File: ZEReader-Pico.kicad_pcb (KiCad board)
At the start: 2 copper layers, 100 x 110 mm, 75 parts, among them J1 Micro_SD_Card_Det2, J2 UART, J3 SWD, J4 Conn_01x24_MountingPin, J5 UJ20-C-H-G-SMT-TR, J6 Conn_01x02_Socket, Q1 Si1308EDL, Q2 DMG2305UX-7, SW1 SW_Push, SW2 SW_Push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

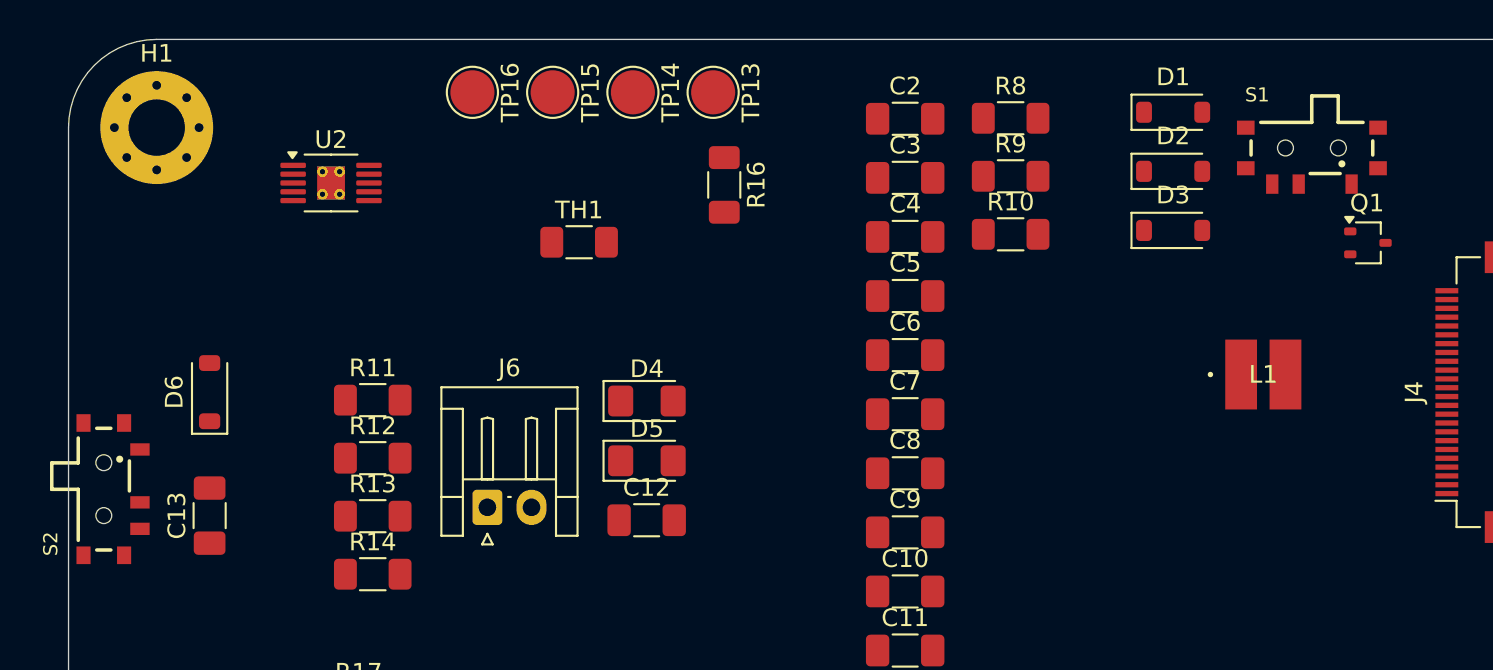
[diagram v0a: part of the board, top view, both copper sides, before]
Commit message: selfcontainment, smaller fixes
Signed-off-by: Anna-Lena Marx <anna-lena.marx@web.de>
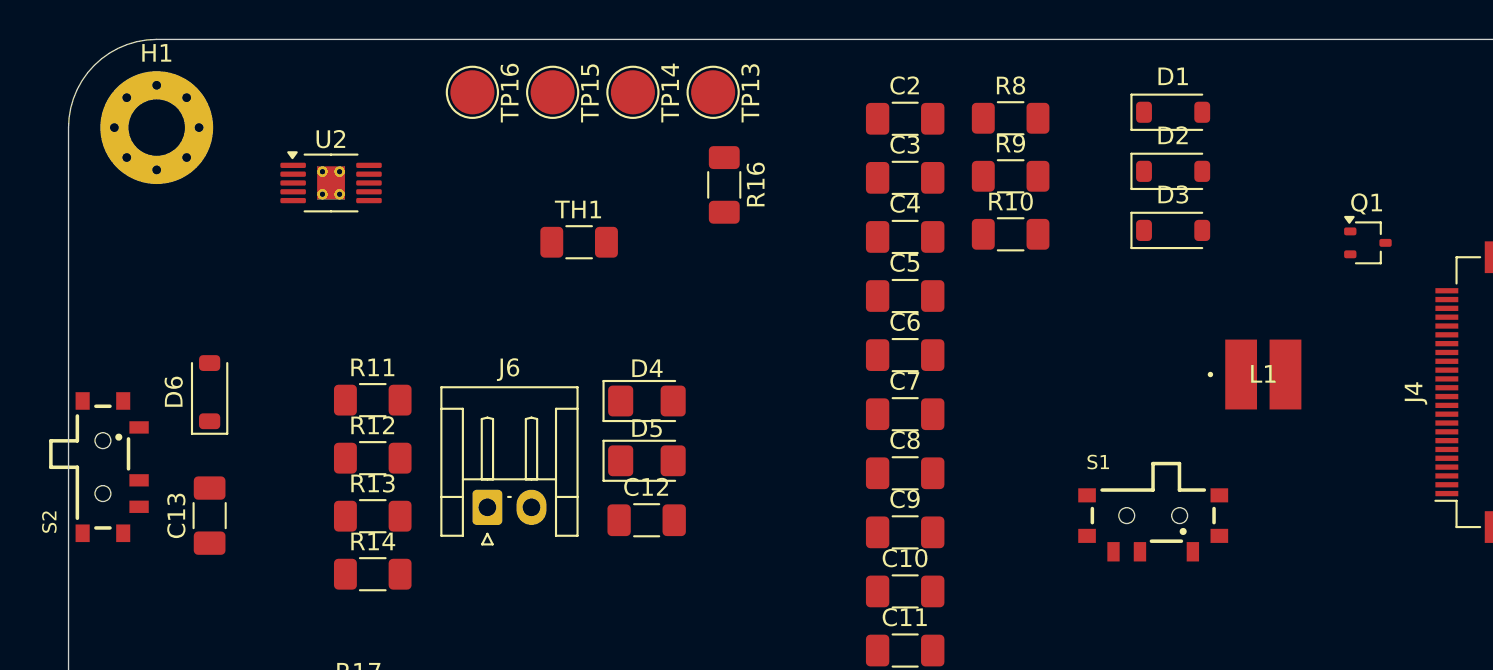
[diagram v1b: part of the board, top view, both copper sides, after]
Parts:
- moved S1 22.7 mm to (111.5, 52.0)
- moved S2 1.25 mm to (52.0, 49.2)

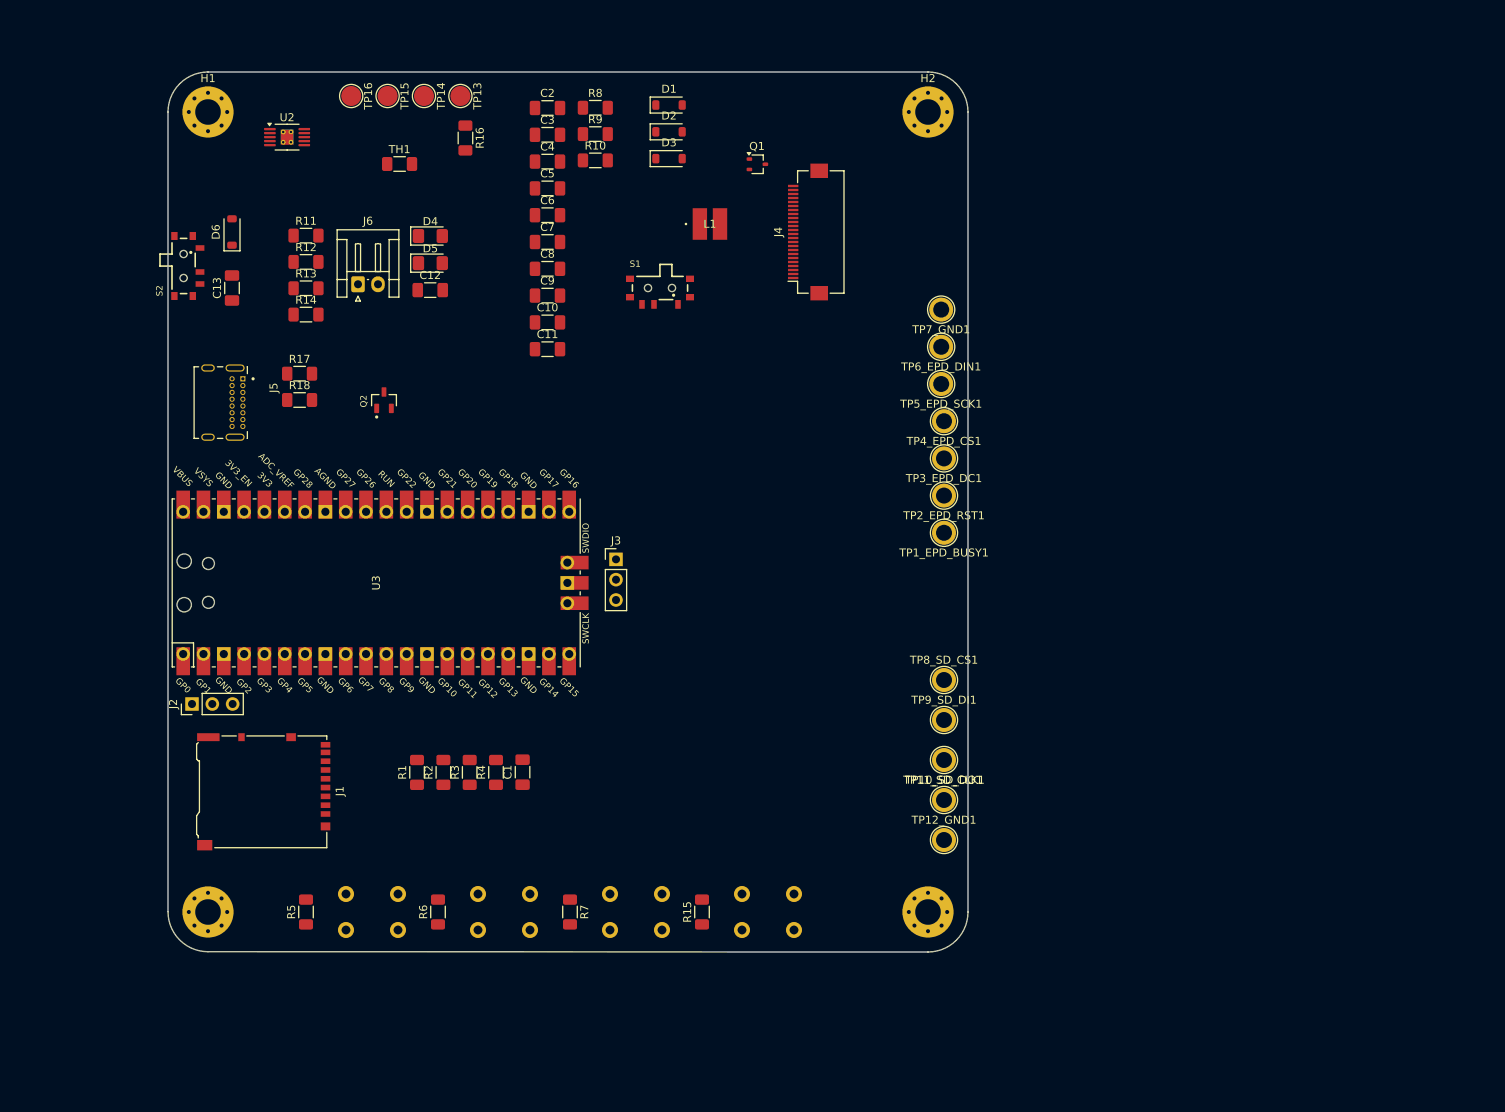
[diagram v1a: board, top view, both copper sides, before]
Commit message: Imported Aisler design rules, routed power and display booster
Signed-off-by: Anna-Lena Marx <anna-lena.marx@web.de>
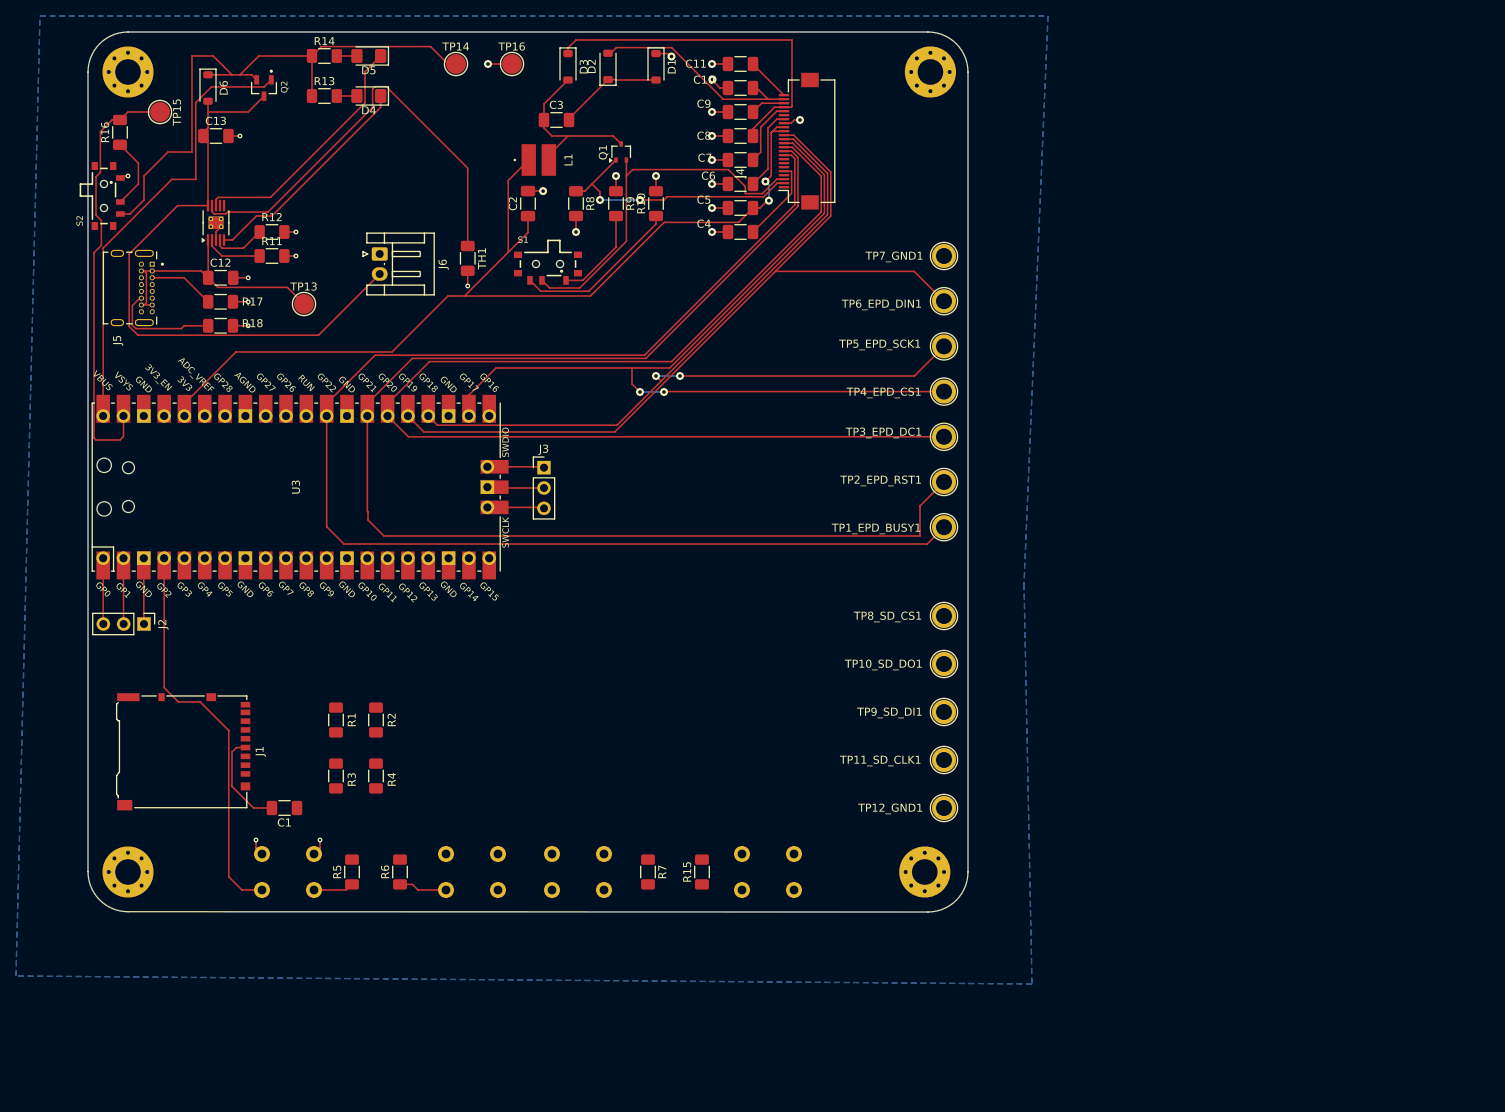
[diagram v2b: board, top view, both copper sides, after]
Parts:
- moved R16 43.2 mm to (44.0, 32.5), turned to 90 degrees
- moved C11 43.0 mm to (121.6, 24.0)
- moved Q2 41.8 mm to (62.0, 27.0), turned to -90 degrees
- moved C10 38.0 mm to (121.6, 27.0)
- moved C9 33.3 mm to (121.6, 30.0)
- moved TP13 32.5 mm to (67.0, 54.0), turned to 0 degrees
- moved R14 32.4 mm to (69.5, 23.0)
- moved C1 30.1 mm to (64.6, 117.0), turned to 180 degrees
- moved C8 29.3 mm to (121.6, 33.0)
- moved TP15 28.5 mm to (49.0, 30.0)
- moved D5 27.0 mm to (75.1, 23.0), turned to 180 degrees
- moved C12 26.2 mm to (56.6, 50.7)
- moved C7 26.2 mm to (121.6, 36.0)
- moved C4 25.7 mm to (121.6, 45.0)
- moved C6 24.4 mm to (121.6, 39.0)
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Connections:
- J2 pad 1: Net-(J2-Pin_1) -> GND
- J2 pad 3: GND -> Net-(J2-Pin_3)
- J6 pad 1: /02_Power/V_USB_LIPO -> GND
- J6 pad 2: GND -> /02_Power/V_USB_LIPO
- U3 pad 1: Net-(J2-Pin_1) -> Net-(J2-Pin_3)
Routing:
- net EPD_BUSY: track 0.00 -> 170.4 mm
- net EPD_RST: track 0.00 -> 164.6 mm
- net /02_Power/V_USB_LIPO: track 0.00 -> 150.3 mm
- net EPD_DC: track 0.00 -> 146.9 mm
- net +3.3V: track 0.00 -> 123.6 mm, vias 0 -> 2
- net EPD_SCK: track 0.00 -> 112.1 mm, vias 0 -> 2
- net EPD_CS: track 0.00 -> 109.4 mm, vias 0 -> 2
- net EPD_DIN: track 0.00 -> 100.7 mm
- net GND: track 0.00 -> 67.5 mm, vias 0 -> 25
- net VBUS: track 0.00 -> 56.3 mm
- net Net-(U2-TS): track 0.00 -> 54.7 mm
- net BTN_1: track 0.00 -> 54.6 mm
- net VSYS: track 0.00 -> 54.2 mm
- net /03_ePaper-Driver/RESE: track 0.00 -> 46.1 mm
- net /03_ePaper-Driver/VGH: track 0.00 -> 44.3 mm
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- added copper zone on B.Cu, net GND
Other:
- board size 100 x 110 mm -> 110 x 110 mm

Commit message: Initial routing finished
Signed-off-by: Anna-Lena Marx <anna-lena.marx@web.de>
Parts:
- moved C1 23.0 mm to (63.4, 94.0), turned to 0 degrees
- moved R5 15.0 mm to (58.0, 125.5)
- moved R3 12.5 mm to (72.0, 100.5), turned to -90 degrees
- moved R4 12.5 mm to (75.5, 100.5), turned to -90 degrees
- moved R2 9.28 mm to (68.5, 100.5), turned to -90 degrees
- moved R1 8.11 mm to (65.0, 100.5), turned to -90 degrees
- moved R15 0.60 mm to (117.0, 125.5), turned to -90 degrees
- moved R6 0.55 mm to (79.0, 125.5)
- moved R7 0.55 mm to (110.0, 125.5)
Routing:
- net +3.3V: track 123.6 -> 314.2 mm
- net SD_DAT3-CD-CS: track 0.00 -> 140.4 mm
- net SD_CLK-SCLK: track 0.00 -> 134.6 mm
- net BTN_4: track 0.00 -> 129.2 mm
- net SD_CMD-DI: track 0.00 -> 125.7 mm
- net BTN_3: track 0.00 -> 124.0 mm
- net SD_DAT0-DO: track 0.00 -> 115.4 mm, vias 0 -> 2
- net BTN_2: track 6.04 -> 95.2 mm
- net Net-(J1-VDD): track 12.3 -> 54.1 mm
- net GND: track 67.5 -> 85.6 mm, vias 25 -> 33
- net BTN_1: track 54.6 -> 64.3 mm
- net EPD_RST: track 164.6 -> 163.5 mm
- net Net-(D5-K): track 31.1 -> 31.6 mm
- net EPD_BUSY: track 170.4 -> 171.0 mm
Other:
- board text added: "ZEReader Pico v1 Git Rev: ${kibot_git-hash} Anna-Lena Marx"
- board text removed: "v1 Git Rev: ${kibot_git-hash}"

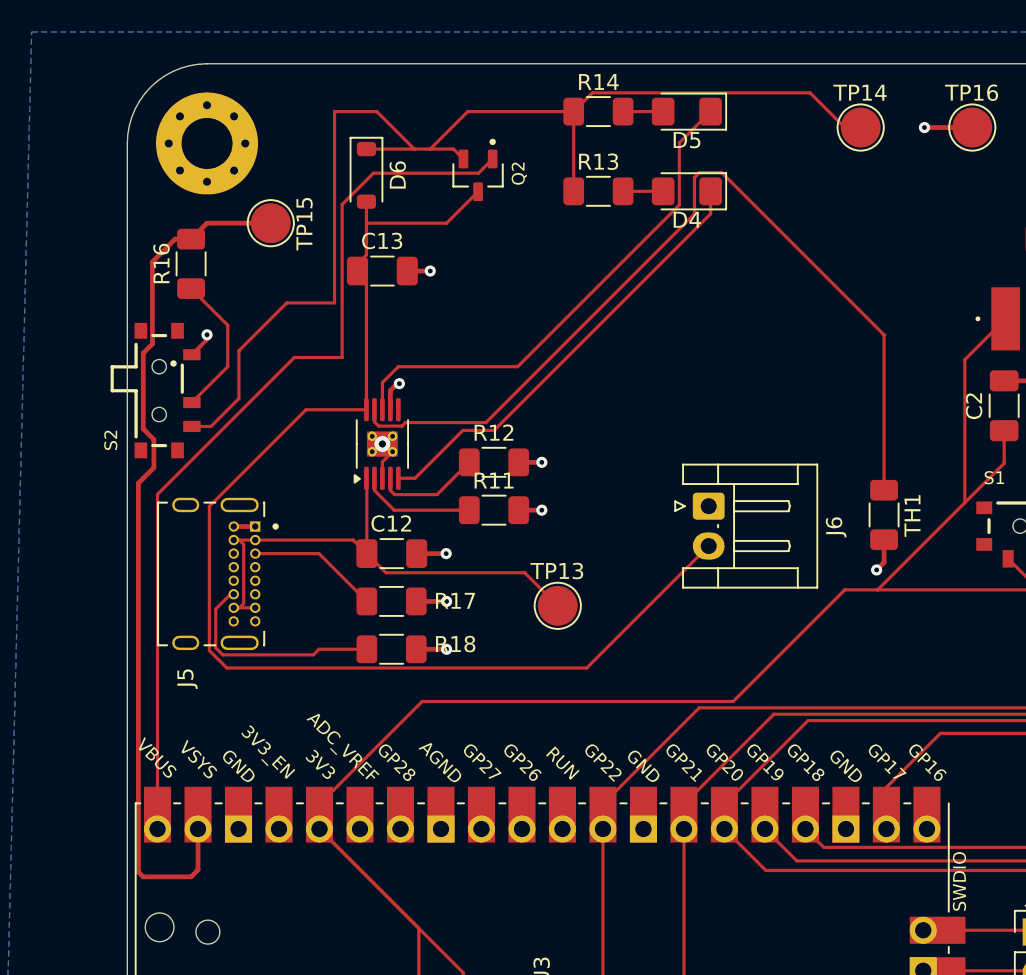
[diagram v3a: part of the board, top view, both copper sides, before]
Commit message: Changed USB connector due to manufacturing rule violations
Signed-off-by: Anna-Lena Marx <anna-lena.marx@web.de>
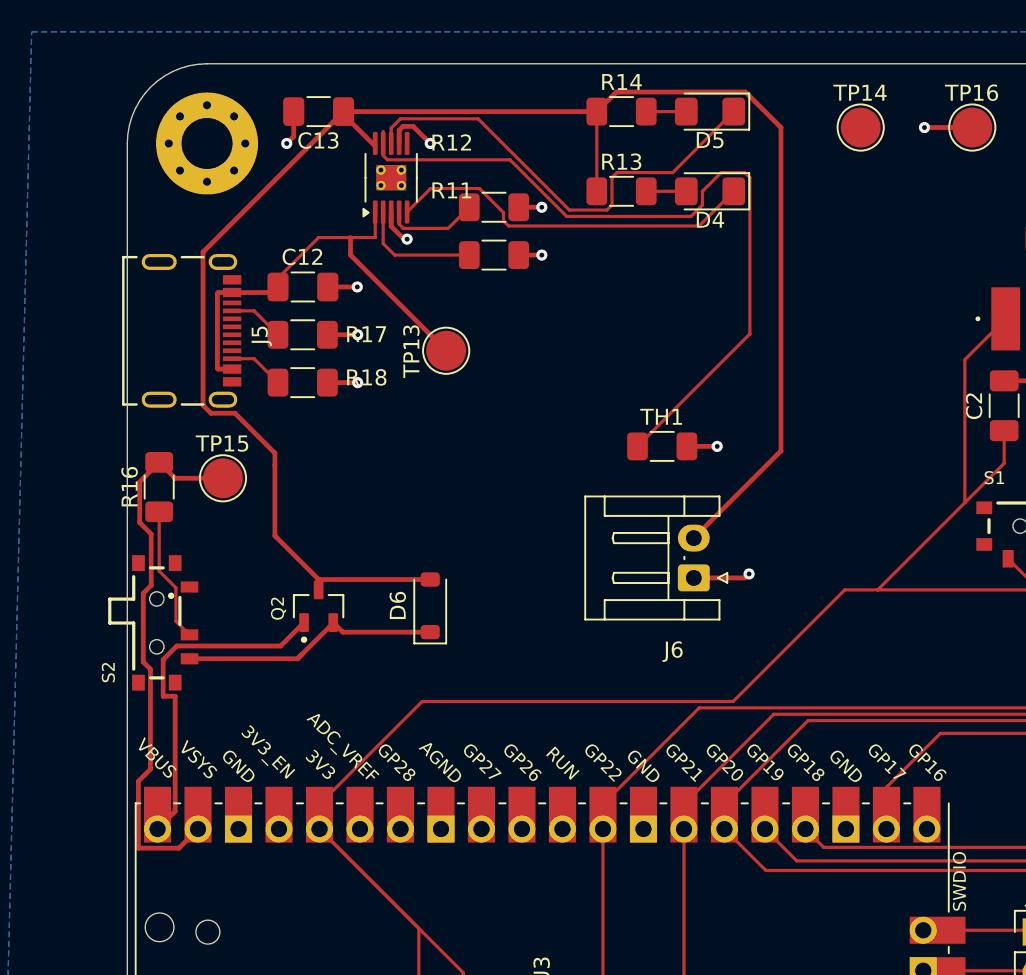
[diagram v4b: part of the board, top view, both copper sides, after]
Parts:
- J5: value UJ20-C-H-G-SMT-TR -> 2171790001; footprint prj-footprints:CUI_UJ20-C-H-G-SMT-TR -> prj-footprints:MOLEX_2171790001
- moved Q2 28.8 mm to (52.0, 54.0), turned to 90 degrees
- moved D6 27.3 mm to (59.0, 54.0), turned to 90 degrees
- moved R17 17.6 mm to (51.0, 37.0)
- moved R18 17.6 mm to (51.0, 40.0)
- moved C12 17.6 mm to (51.0, 34.0)
- moved TP13 17.5 mm to (60.0, 38.0), turned to 90 degrees
- moved U2 16.7 mm to (56.5, 27.1)
- moved TP15 16.3 mm to (46.0, 46.0), turned to 0 degrees
- moved R11 16.0 mm to (63.0, 32.0)
- moved R12 16.0 mm to (63.0, 29.0)
- moved J5 15.3 mm to (43.1, 36.8)
- moved S2 14.6 mm to (41.9, 55.1)
- moved TH1 14.6 mm to (73.5, 44.0), turned to 0 degrees
- moved R16 14.1 mm to (42.0, 46.5)
- moved C13 10.8 mm to (52.0, 23.0), turned to 180 degrees
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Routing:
- net VBUS: track 56.3 -> 21.6 mm
- net /02_Power/V_USB_LIPO: track 150.3 -> 127.1 mm
- net VSYS: track 54.2 -> 34.4 mm
- net Net-(J5-CC2): track 13.8 -> 3.50 mm
- net Net-(U2-TS): track 54.7 -> 47.6 mm
- net Net-(J5-CC1): track 8.24 -> 3.50 mm
- net Net-(D4-K): track 27.9 -> 23.3 mm
- net /02_Power/USB_VBUS: track 33.0 -> 28.5 mm
- net Net-(D5-K): track 31.6 -> 28.6 mm
- net Net-(U2-PRETERM): track 6.66 -> 5.82 mm
- net Net-(R16-Pad1): track 9.03 -> 8.51 mm

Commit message: Worked on Design, eliminating errors
Signed-off-by: Anna-Lena Marx <anna-lena.marx@web.de>
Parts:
- added G***: LOGO, prj-footprints:Logo, F.Cu at (96.0, 107.0)
- added G***: LOGO, prj-footprints:Logo-small, B.Cu at (135.0, 125.0)
- J6: footprint Connector_JST:JST_EH_S2B-EH_1x02_P2.50mm_Horizontal -> Connector_JST:JST_PH_S2B-PH-K_1x02_P2.00mm_Horizontal
- moved TH1 54.9 mm to (117.5, 77.0)
- moved J6 7.06 mm to (69.5, 56.0)
- moved D6 2.00 mm to (57.0, 54.0)
- moved S1 0.29 mm to (97.2, 48.9)
- renumbered TP13 to TP13_USB_VBUS1, TP14 to TP14_USB_LIPO1, TP15 to TP15_VSYS1, TP16 to TP16_GND1
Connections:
- J6 pad 1: GND -> /02_Power/V_USB_LIPO
- J6 pad 2: /02_Power/V_USB_LIPO -> GND
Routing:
- net Net-(U2-TS): track 47.6 -> 129.2 mm, vias 0 -> 6
- net /02_Power/V_USB_LIPO: track 127.1 -> 135.5 mm
- net GND: track 85.1 -> 90.2 mm, vias 33 -> 36
- net +3.3V: track 314.2 -> 313.7 mm
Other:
- board text added: "+ -"
- board text added: "CHARGING"
- board text added: "CON"
- board text added: "GND"
- board text added: "RX"
- board text added: "SWCLK"
- board text added: "SWDIO"
- board text added: "TX"

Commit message: updated KiBot tasks
Signed-off-by: Anna-Lena Marx <anna-lena.marx@web.de>
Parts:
- moved R6 63.7 mm to (139.5, 145.6)
- moved SW2 63.7 mm to (151.8, 142.8)
- moved D4 63.3 mm to (136.6, 48.0)
- moved D5 63.3 mm to (136.6, 43.0)
- moved J6 63.3 mm to (129.6, 76.0)
- moved R2 63.3 mm to (128.6, 120.5)
- moved R4 63.3 mm to (135.6, 120.5)
- moved J5 63.3 mm to (103.2, 56.8)
- moved C1 63.3 mm to (123.5, 114.0)
- moved C10 63.3 mm to (181.7, 47.0)
- moved C11 63.3 mm to (181.7, 44.0)
- moved C12 63.3 mm to (111.1, 54.0)
- moved C13 63.3 mm to (112.1, 43.0)
- moved C2 63.3 mm to (155.1, 61.5)
- moved C3 63.3 mm to (158.7, 51.0)
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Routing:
- net +3.3V: track 313.7 -> 314.4 mm
